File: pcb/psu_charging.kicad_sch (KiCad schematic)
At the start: 23 parts, among them J1 BATT+, J1 USB4105-GF-A, J2 GND, J4 VBUS, J6 S2B-PH-K/DNP, J7 GND, U1 AP2112K-3.3, U4 MCP73831/OT

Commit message: Refactored details component namings + bom excludings
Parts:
- BT1: value Battery_Cell -> 1042P
- D1: value LED_Small -> LED_RED
- D2: value RED -> LED_RED
- D3: value GREEN -> LED_GREEN
- J6, JP1: now left out of the parts list
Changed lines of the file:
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@@
       (effects (font (size 1.27 1.27)))
     )
-    (property "Value" "GREEN" (at 242.57 85.2424 0)
+    (property "Value" "LED_GREEN" (at 242.57 85.2424 0)
       (effects (font (size 1.27 1.27)))
     )
@@
   )
   (symbol (lib_id "Jumper:SolderJumper_2_Open") (at 68.58 93.98 0) (unit 1)
-    (in_bom yes) (on_board yes) (dnp no) (fields_autoplaced)
+    (in_bom no) (on_board yes) (dnp no) (fields_autoplaced)
     (property "Reference" "JP1" (at 68.58 90.0811 0)
       (effects (font (size 1.27 1.27)))
@@
       (effects (font (size 1.27 1.27)))
     )
-    (property "Value" "RED" (at 242.57 77.0636 0)
+    (property "Value" "LED_RED" (at 242.57 77.0636 0)
       (effects (font (size 1.27 1.27)))
     )
@@
       (effects (font (size 1.27 1.27)) (justify left))
     )
-    (property "Value" "Battery_Cell" (at 138.811 93.2253 0)
+    (property "Value" "1042P" (at 138.811 93.2253 0)
       (effects (font (size 1.27 1.27)) (justify left))
     )
@@
       (effects (font (size 1.27 1.27)))
     )
-    (property "Value" "LED_Small" (at 54.5465 46.1551 0)
+    (property "Value" "LED_RED" (at 54.5465 46.1551 0)
       (effects (font (size 1.27 1.27)))
     )
@@
   )
   (symbol (lib_id "Connector:Conn_01x02_Pin") (at 161.29 92.71 0) (unit 1)
-    (in_bom yes) (on_board yes) (dnp no)
+    (in_bom no) (on_board yes) (dnp no)
     (property "Reference" "J6" (at 160.02 86.36 0)
       (effects (font (size 1.27 1.27)))

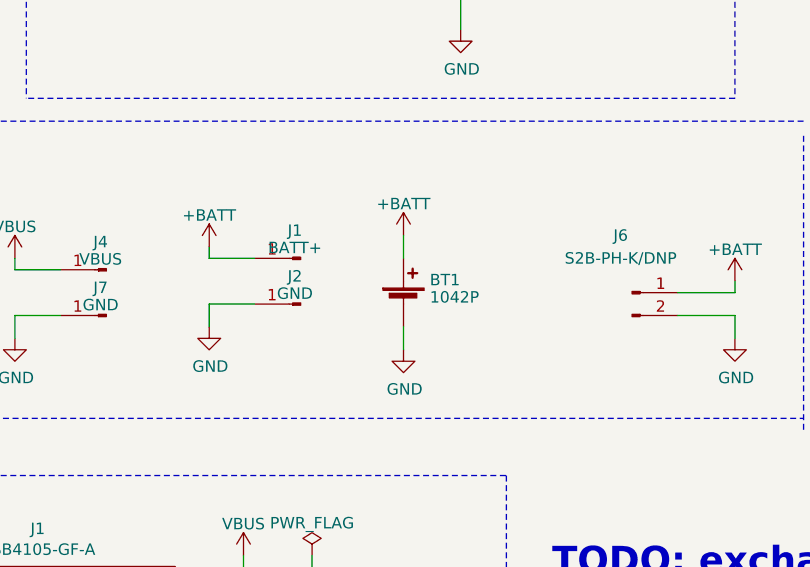
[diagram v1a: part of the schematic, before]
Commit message: Applied ERC issue changes + DRC issues fix
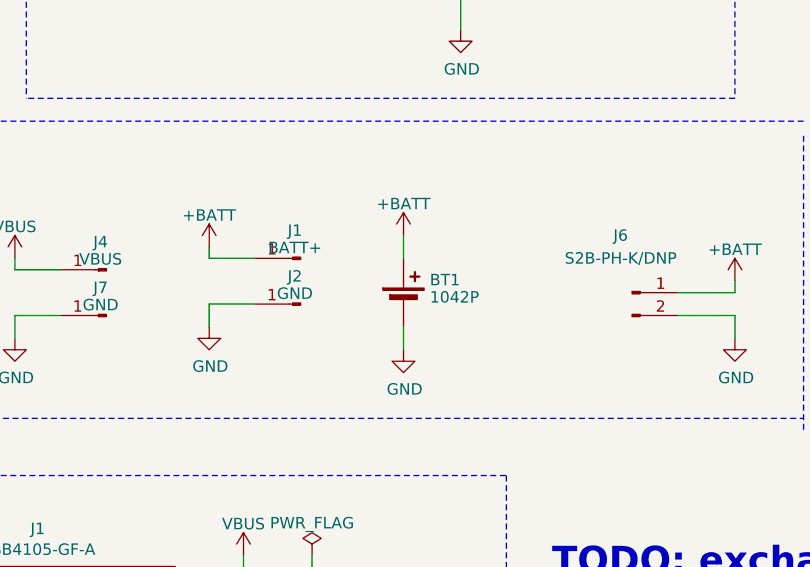
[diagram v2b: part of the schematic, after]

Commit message: Added notes and ToDos to be worked on for REV.02
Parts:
- added R2: 10k, Resistor_SMD:R_0603_1608Metric, symbol Device:R
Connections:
- net +BATT: no longer D2.2 (A)
- net ENABLE: now also R2.2
- net GND: now also R2.1
- net VBUS: now also D2.2 (A)
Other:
- note added: "18650 GARBAGE HOLDER!!!!"
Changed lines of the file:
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@@
   (junction (at 252.73 53.34) (diameter 0) (color 0 0 0 0)
   )
+  (junction (at 142.24 62.23) (diameter 0) (color 0 0 0 0)
+  )
   (junction (at 154.94 46.99) (diameter 0) (color 0 0 0 0)
   )
-  (junction (at 142.24 59.69) (diameter 0) (color 0 0 0 0)
+  (junction (at 128.905 49.53) (diameter 0) (color 0 0 0 0)
   )
   (junction (at 118.11 125.73) (diameter 0) (color 0 0 0 0)
@@
     (stroke (width 0) (type default))
   )
+  (wire (pts (xy 128.905 60.96) (xy 128.905 64.135))
+    (stroke (width 0) (type default))
+  )
   (wire (pts (xy 92.71 95.25) (xy 92.71 97.79))
     (stroke (width 0) (type default))
@@
     (stroke (width 0) (type default))
   )
-  (wire (pts (xy 124.46 49.53) (xy 134.62 49.53))
+  (wire (pts (xy 124.46 49.53) (xy 128.905 49.53))
     (stroke (width 0) (type default))
   )
@@
     (stroke (width 0) (type default))
   )
-  (wire (pts (xy 130.81 59.69) (xy 142.24 59.69))
-    (stroke (width 0) (type default))
-  )
   (wire (pts (xy 219.71 44.45) (xy 219.71 45.72))
     (stroke (width 0) (type default))
@@
     (stroke (width 0) (type default))
   )
-  (wire (pts (xy 130.81 57.15) (xy 130.81 59.69))
-    (stroke (width 0) (type default))
-  )
-  (wire (pts (xy 142.24 57.15) (xy 142.24 59.69))
+  (wire (pts (xy 142.24 57.15) (xy 142.24 62.23))
     (stroke (width 0) (type default))
   )
@@
   )
   (wire (pts (xy 160.02 46.99) (xy 154.94 46.99))
+    (stroke (width 0) (type default))
+  )
+  (wire (pts (xy 128.905 49.53) (xy 134.62 49.53))
     (stroke (width 0) (type default))
   )
@@
     (stroke (width 0) (type dash))
   )
+  (wire (pts (xy 137.16 61.595) (xy 137.16 62.23))
+    (stroke (width 0) (type default))
+  )
   (wire (pts (xy 154.94 48.26) (xy 154.94 46.99))
     (stroke (width 0) (type default))
   )
   (wire (pts (xy 72.39 93.98) (xy 82.55 93.98))
+    (stroke (width 0) (type default))
+  )
+  (wire (pts (xy 137.16 62.23) (xy 142.24 62.23))
     (stroke (width 0) (type default))
   )
@@
     (stroke (width 0) (type default))
   )
+  (wire (pts (xy 142.24 62.23) (xy 142.24 63.5))
+    (stroke (width 0) (type default))
+  )
   (polyline (pts (xy 274.32 26.67) (xy 274.32 100.33))
     (stroke (width 0) (type dash))
@@
     (stroke (width 0) (type default))
   )
+  (wire (pts (xy 128.905 49.53) (xy 128.905 53.34))
+    (stroke (width 0) (type default))
+  )
   (wire (pts (xy 114.3 93.98) (xy 114.3 96.52))
     (stroke (width 0) (type default))
@@
   )
   (wire (pts (xy 213.36 58.42) (xy 210.82 58.42))
-    (stroke (width 0) (type default))
-  )
-  (wire (pts (xy 142.24 59.69) (xy 142.24 63.5))
     (stroke (width 0) (type default))
   )
@@
     (effects (font (size 1.27 1.27)) (justify left bottom))
   )
+  (text "18650 GARBAGE HOLDER!!!!" (at 107.315 94.615 0)
+    (effects (font (size 3 3) (thickness 0.6) bold) (justify left bottom))
+  )
   (text "USB-C" (at 53.34 116.84 0)
     (effects (font (size 1.27 1.27)) (justify left bottom))
@@
         (path "/b363dc8f-4a45-4779-a397-ccb82393dab8/eebb1d37-a01d-4adf-be70-a8e8f9293475/23008b32-6835-495f-a93f-d60d3125c4cb"
           (reference "J2") (unit 1)
+        )
+      )
+    )
+  )
+  (symbol (lib_id "Device:R") (at 128.905 57.15 180) (unit 1)
+    (in_bom yes) (on_board yes) (dnp no)
+    (property "Reference" "R2" (at 127.127 58.3184 0)
+      (effects (font (size 1.27 1.27)) (justify left))
+    )
+    (property "Value" "10k" (at 127.127 56.007 0)
+      (effects (font (size 1.27 1.27)) (justify left))
+    )
+    (property "Footprint" "Resistor_SMD:R_0603_1608Metric" (at 130.683 57.15 90)
+      (effects (font (size 1.27 1.27)) hide)
+    )
+    (property "Datasheet" "~" (at 128.905 57.15 0)
+      (effects (font (size 1.27 1.27)) hide)
+    )
+    (pin "1")
+    (pin "2")
+    (instances
+      (project "RP2040_minimal"
+        (path "/966e07a3-e14e-42ec-8301-447655da419c"
+          (reference "R2") (unit 1)
+        )
+      )
+      (project "rep-trap-pcb"
+        (path "/b363dc8f-4a45-4779-a397-ccb82393dab8/eebb1d37-a01d-4adf-be70-a8e8f9293475/e7ccec12-46ad-495a-887c-7169982423a2"
+          (reference "R18") (unit 1)
+        )
+        (path "/b363dc8f-4a45-4779-a397-ccb82393dab8/eebb1d37-a01d-4adf-be70-a8e8f9293475/23008b32-6835-495f-a93f-d60d3125c4cb"
+          (reference "R19") (unit 1)
         )
       )
@@
     )
   )
-  (symbol (lib_id "power:+BATT") (at 234.95 78.74 0) (unit 1)
-    (in_bom yes) (on_board yes) (dnp no) (fields_autoplaced)
-    (property "Reference" "#PWR020" (at 234.95 82.55 0)
-      (effects (font (size 1.27 1.27)) hide)
-    )
-    (property "Value" "+BATT" (at 234.95 75.2381 0)
-      (effects (font (size 1.27 1.27)))
-    )
-    (property "Footprint" "" (at 234.95 78.74 0)
-      (effects (font (size 1.27 1.27)) hide)
-    )
-    (property "Datasheet" "" (at 234.95 78.74 0)
-      (effects (font (size 1.27 1.27)) hide)
-    )
-    (pin "1")
-    (instances
-      (project "rep-trap-pcb"
-        (path "/b363dc8f-4a45-4779-a397-ccb82393dab8/eebb1d37-a01d-4adf-be70-a8e8f9293475/23008b32-6835-495f-a93f-d60d3125c4cb"
-          (reference "#PWR020") (unit 1)
-        )
-      )
-    )
-  )
   (symbol (lib_id "Device:R_Small") (at 251.46 88.9 270) (unit 1)
     (in_bom yes) (on_board yes) (dnp no)
@@
     )
   )
+  (symbol (lib_id "power:VBUS") (at 234.95 78.74 0) (unit 1)
+    (in_bom yes) (on_board yes) (dnp no) (fields_autoplaced)
+    (property "Reference" "#PWR020" (at 234.95 82.55 0)
+      (effects (font (size 1.27 1.27)) hide)
+    )
+    (property "Value" "VBUS" (at 234.95 75.2381 0)
+      (effects (font (size 1.27 1.27)))
+    )
+    (property "Footprint" "" (at 234.95 78.74 0)
+      (effects (font (size 1.27 1.27)) hide)
+    )
+    (property "Datasheet" "" (at 234.95 78.74 0)
+      (effects (font (size 1.27 1.27)) hide)
+    )
+    (pin "1")
+    (instances
+      (project "rep-trap-pcb"
+        (path "/b363dc8f-4a45-4779-a397-ccb82393dab8/eebb1d37-a01d-4adf-be70-a8e8f9293475/23008b32-6835-495f-a93f-d60d3125c4cb"
+          (reference "#PWR020") (unit 1)
+        )
+      )
+    )
+  )
   (symbol (lib_id "Device:Battery_Cell") (at 135.89 93.98 0) (unit 1)
     (in_bom yes) (on_board yes) (dnp no) (fields_autoplaced)
-    (property "Reference" "BT1" (at 138.811 91.3043 0)
+    (property "Reference" "BT1" (at 139.7 90.8685 0)
       (effects (font (size 1.27 1.27)) (justify left))
     )
-    (property "Value" "1042P" (at 138.811 93.2253 0)
+    (property "Value" "1042P" (at 139.7 93.4085 0)
       (effects (font (size 1.27 1.27)) (justify left))
     )
@@
     )
   )
-  (symbol (lib_id "power:PWR_FLAG") (at 130.81 57.15 0) (unit 1)
+  (symbol (lib_id "power:PWR_FLAG") (at 137.16 61.595 0) (unit 1)
     (in_bom yes) (on_board yes) (dnp no) (fields_autoplaced)
-    (property "Reference" "#FLG0102" (at 130.81 55.245 0)
-      (effects (font (size 1.27 1.27)) hide)
-    )
-    (property "Value" "PWR_FLAG" (at 130.81 53.5455 0)
-      (effects (font (size 1.27 1.27)))
-    )
-    (property "Footprint" "" (at 130.81 57.15 0)
-      (effects (font (size 1.27 1.27)) hide)
-    )
-    (property "Datasheet" "~" (at 130.81 57.15 0)
+    (property "Reference" "#FLG0102" (at 137.16 59.69 0)
+      (effects (font (size 1.27 1.27)) hide)
+    )
+    (property "Value" "PWR_FLAG" (at 137.16 57.9905 0)
+      (effects (font (size 1.27 1.27)))
+    )
+    (property "Footprint" "" (at 137.16 61.595 0)
+      (effects (font (size 1.27 1.27)) hide)
+    )
+    (property "Datasheet" "~" (at 137.16 61.595 0)
       (effects (font (size 1.27 1.27)) hide)
     )
@@
         )
       )
+    )
+  )
+  (symbol (lib_id "power:GND") (at 128.905 64.135 0) (unit 1)
+    (in_bom yes) (on_board yes) (dnp no)
+    (property "Reference" "#PWR0111" (at 128.905 70.485 0)
+      (effects (font (size 1.27 1.27)) hide)
+    )
+    (property "Value" "GND" (at 129.032 68.5292 0)
+      (effects (font (size 1.27 1.27)))
+    )
+    (property "Footprint" "" (at 128.905 64.135 0)
+      (effects (font (size 1.27 1.27)) hide)
+    )
+    (property "Datasheet" "" (at 128.905 64.135 0)
+      (effects (font (size 1.27 1.27)) hide)
+    )
+    (pin "1")
+    (instances
+      (project "trick-tracker"
+        (path "/a8447faf-e0a0-4c4a-ae53-4d4b28669151"
+          (reference "#PWR0111") (unit 1)
+        )
+      )
+      (project "rep-trap-pcb"
+        (path "/b363dc8f-4a45-4779-a397-ccb82393dab8/eebb1d37-a01d-4adf-be70-a8e8f9293475/23008b32-6835-495f-a93f-d60d3125c4cb"
+          (reference "#PWR070") (unit 1)
+        )
+      )

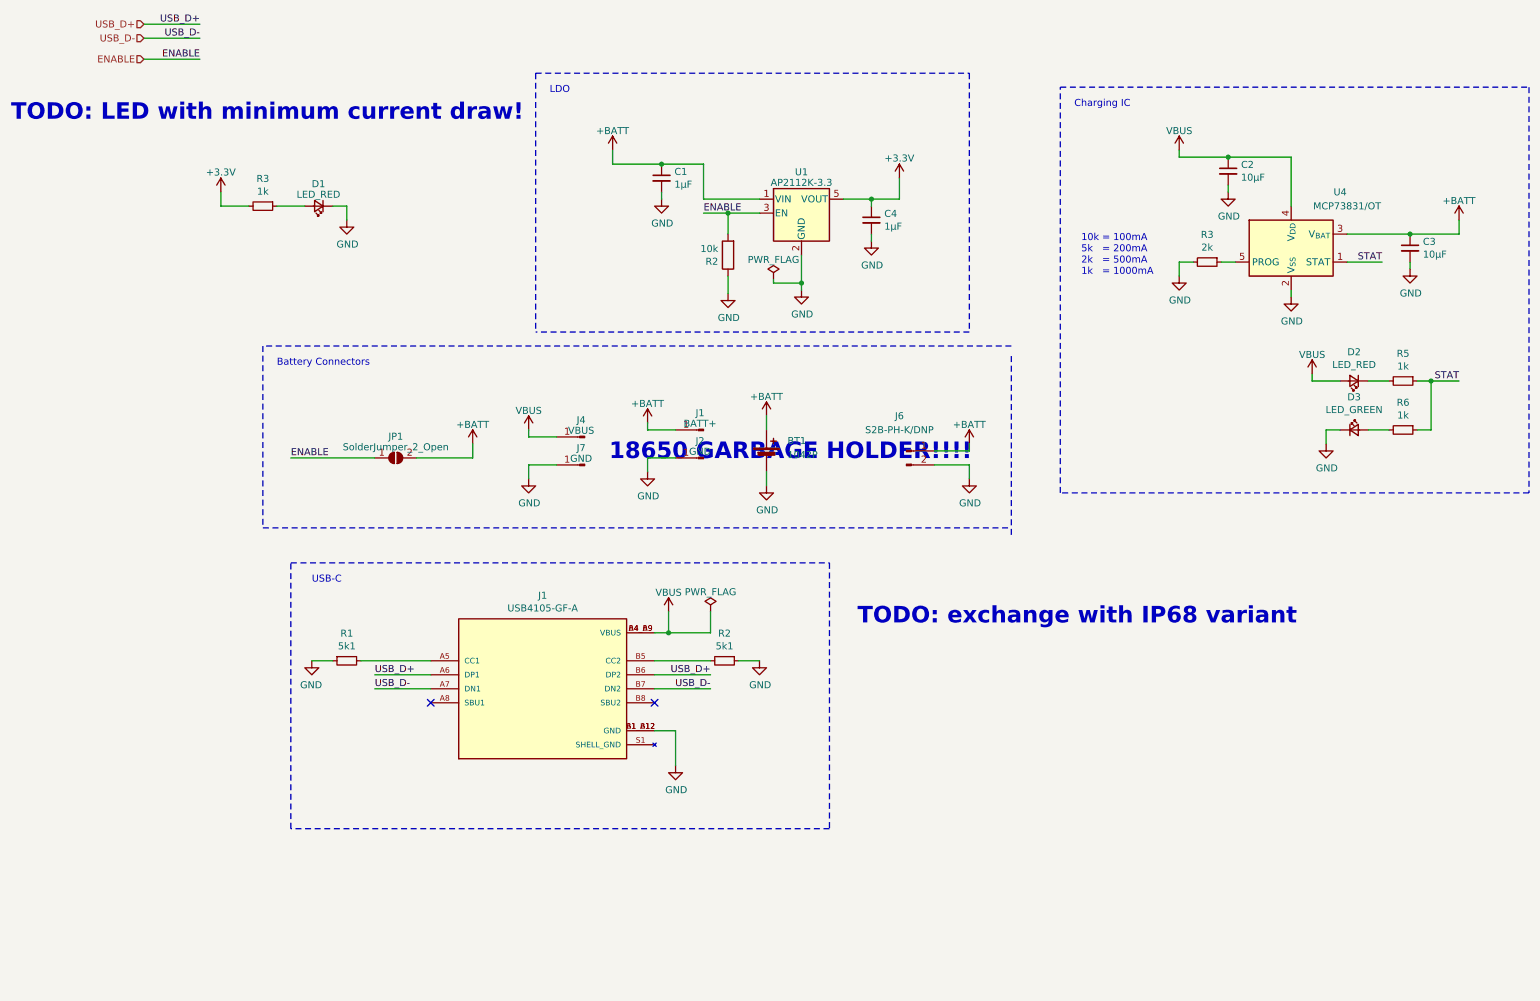
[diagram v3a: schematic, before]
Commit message: refactored components and layout
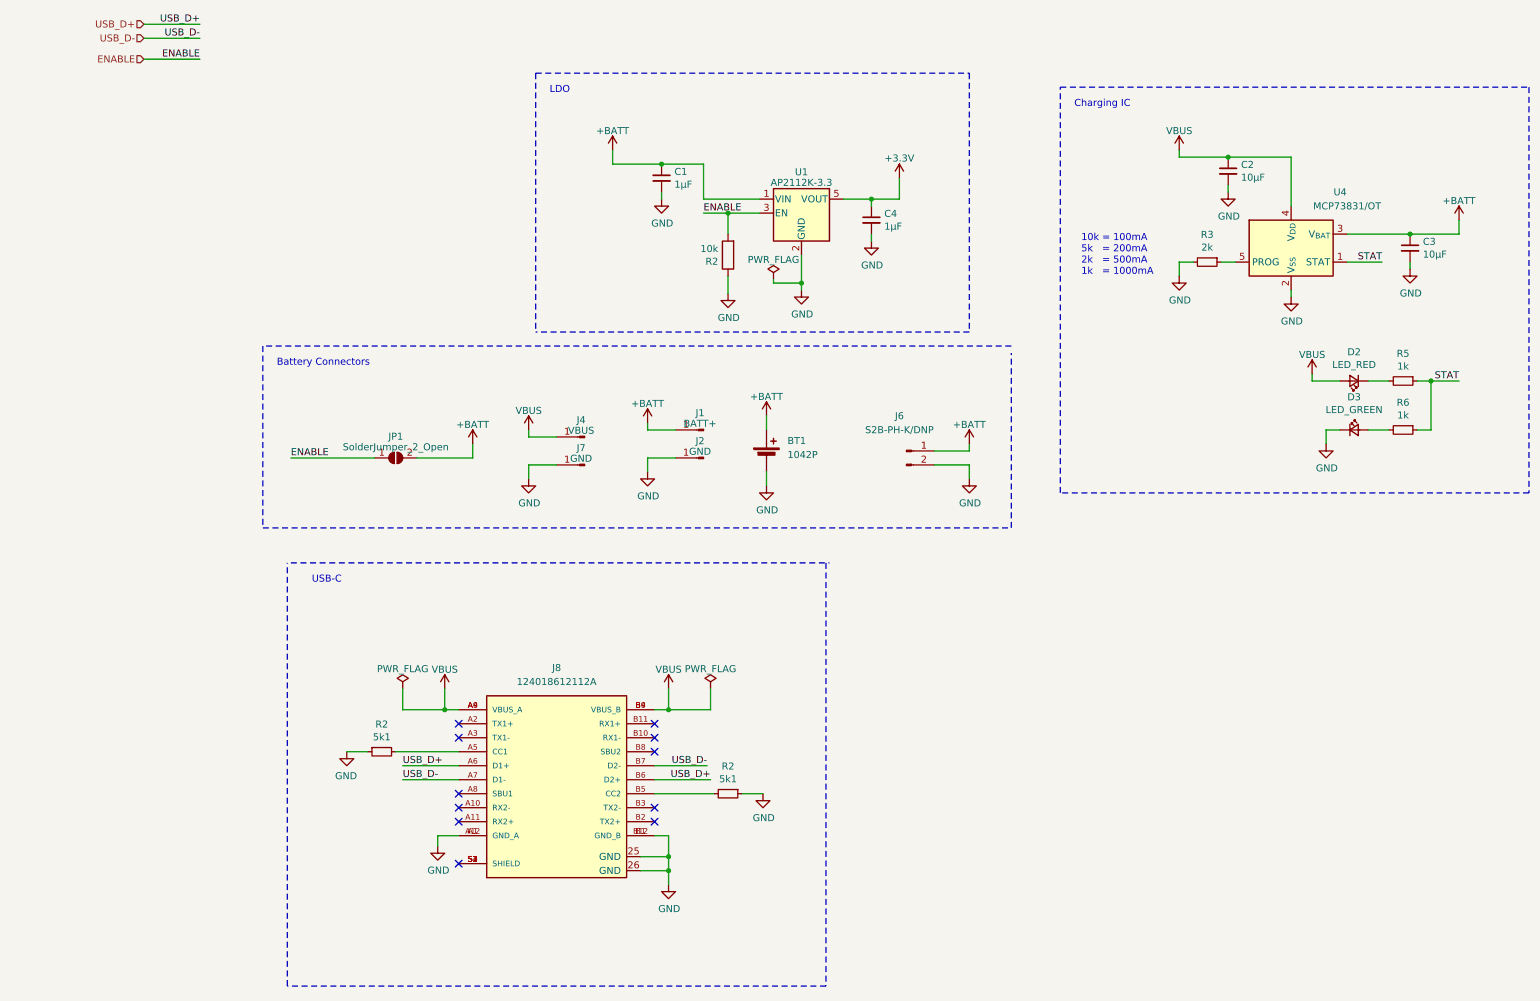
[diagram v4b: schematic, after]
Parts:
- removed D1: LED_RED, LED_SMD:LED_0603_1608Metric, symbol Device:LED_Small
- removed J1: USB4105-GF-A, USB4105-GF-A:GCT_USB4105-GF-A, symbol USB4105-GF-A:USB4105-GF-A
- removed R1, R2: 5k1, Resistor_SMD:R_0603_1608Metric, symbol Device:R_Small
- removed R3: 1k, Resistor_SMD:R_0603_1608Metric, symbol Device:R_Small
- added J8: 124018612112A, 124018612112A:CONN_124018612112A_AMP, symbol 124019572112A:124019572112A
- added R2 (x2): 5k1, Resistor_SMD:R_0603_1608Metric, symbol Device:R_Small
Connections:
- net GND: now also J8.25 (GND), J8.26 (GND), J8.A1 (GND_A), J8.A12 (GND_A), J8.B1 (GND_B), J8.B12 (GND_B), R2.1, R2.1
- net USB_D+: now also J8.A6 (D1+), J8.B6 (D2+)
- net USB_D-: now also J8.A7 (D1-), J8.B7 (D2-)
- net VBUS: now also J8.A4 (VBUS_A), J8.A9 (VBUS_A), J8.B4 (VBUS_B), J8.B9 (VBUS_B)
- new net: J8.A5 (CC1), R2.2
- new net: J8.B5 (CC2), R2.2
- new net: J8.S1 (SHIELD), J8.S2 (SHIELD), J8.S3 (SHIELD), J8.S4 (SHIELD)
- no-connect marks 2 -> 11
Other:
- note removed: "18650 GARBAGE HOLDER!!!!"
- note removed: "TODO: LED with minimum current draw!"
- note removed: "TODO: exchange with IP68 variant"
